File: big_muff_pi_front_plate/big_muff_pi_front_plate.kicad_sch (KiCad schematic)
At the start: 13 parts, among them J1 top_panel_connector

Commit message: Potentiometers checked, LED updated
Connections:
- net 0: now also J1.3 (GND)
- net at J1.5 (Pin_5): now also RV2.3; no longer RV2.1
- net at J1.9 (Pin_9): now also RV2.1; no longer RV2.3
- net at RV3.1: now also J1.16 (Pin_16); no longer J1.12 (Pin_12)
- net at RV3.3: now also J1.12 (Pin_12); no longer J1.16 (Pin_16)
- net 9V: now reaches J1.1 (VCC)
- net at J1.2 (Pin_2): now also RV1.3; no longer RV1.1
- net at J1.6 (Pin_6): now also RV1.1; no longer RV1.3
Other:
- moved on the sheet: RV1, RV2, RV3
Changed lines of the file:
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@@
+	(wire
+		(pts
+			(xy 238.76 124.46) (xy 236.22 124.46)
+		)
+		(stroke
+			(width 0)
+			(type default)
+		)
+	)
 	(wire
 		(pts
@@
 	(wire
 		(pts
+			(xy 236.22 124.46) (xy 236.22 128.27)
+		)
+		(stroke
+			(width 0)
+			(type default)
+		)
+	)
+	(wire
+		(pts
 			(xy 124.46 152.4) (xy 124.46 158.75)
 		)
@@
 			(width 0)
 			(type default)
+		)
+	)
+	(wire
+		(pts
+			(xy 236.22 140.97) (xy 236.22 144.78)
+		)
+		(stroke
+			(width 0)
+			(type default)
+		)
+	)
+	(global_label "9V"
+		(shape output)
+		(at 238.76 124.46 0)
+		(fields_autoplaced yes)
+		(effects
+			(font
+				(size 1.27 1.27)
+			)
+			(justify left)
+		)
+		(property "Intersheetrefs" "${INTERSHEET_REFS}"
+			(at 244.0433 124.46 0)
+			(effects
+				(font
+					(size 1.27 1.27)
+				)
+				(justify left)
+				(hide yes)
+			)
 		)
 	)
@@
 	)
 	(symbol
+		(lib_id "Simulation_SPICE:0")
+		(at 236.22 144.78 0)
+		(unit 1)
+		(exclude_from_sim no)
+		(in_bom yes)
+		(on_board yes)
+		(dnp no)
+		(fields_autoplaced yes)
+		(property "Reference" "#GND023"
+			(at 236.22 147.32 0)
+			(effects
+				(font
+					(size 1.27 1.27)
+				)
+				(hide yes)
+			)
+		)
+		(property "Value" "0"
+			(at 236.22 142.875 0)
+			(effects
+				(font
+					(size 1.27 1.27)
+				)
+				(hide yes)
+			)
+		)
+		(property "Footprint" ""
+			(at 236.22 144.78 0)
+			(effects
+				(font
+					(size 1.27 1.27)
+				)
+				(hide yes)
+			)
+		)
+		(property "Datasheet" "~"
+			(at 236.22 144.78 0)
+			(effects
+				(font
+					(size 1.27 1.27)
+				)
+				(hide yes)
+			)
+		)
+		(property "Description" ""
+			(at 236.22 144.78 0)
+			(effects
+				(font
+					(size 1.27 1.27)
+				)
+			)
+		)
+		(pin "1"
+		)
+		(instances
+			(project "big_muff_pi_front_plate"
+				(path "/1fda0e48-ac05-4486-b24b-352a2425b266"
+					(reference "#GND023")
+					(unit 1)
+				)
+			)
+		)
+	)
+	(symbol
 		(lib_id "Device:R_Potentiometer")
-		(at 54.61 77.47 0)
-		(mirror y)
+		(at 54.61 77.47 180)
 		(unit 1)
 		(exclude_from_sim no)
@@
 		(on_board yes)
 		(dnp no)
-		(fields_autoplaced yes)
 		(property "Reference" "RV3"
-			(at 57.15 76.1999 0)
+			(at 57.15 78.7401 0)
 			(effects
 				(font
@@
 		)
 		(property "Value" "R_Potentiometer"
-			(at 57.15 78.7399 0)
+			(at 57.15 76.2001 0)
 			(effects
 				(font
@@
 	(symbol
 		(lib_id "Device:R_Potentiometer")
-		(at 54.61 55.88 0)
-		(mirror y)
+		(at 54.61 55.88 180)
 		(unit 1)
 		(exclude_from_sim no)
@@
 		(on_board yes)
 		(dnp no)
-		(fields_autoplaced yes)
 		(property "Reference" "RV2"
-			(at 57.15 54.6099 0)
+			(at 57.15 57.1501 0)
 			(effects
 				(font
@@
 		)
 		(property "Value" "R_Potentiometer"
-			(at 57.15 57.1499 0)
+			(at 57.15 54.6101 0)
 			(effects
 				(font
@@
 	(symbol
 		(lib_id "Device:R_Potentiometer")
-		(at 54.61 33.02 0)
-		(mirror y)
+		(at 54.61 33.02 180)
 		(unit 1)
 		(exclude_from_sim no)
@@
 		(on_board yes)
 		(dnp no)
-		(fields_autoplaced yes)
 		(property "Reference" "RV1"
-			(at 57.15 31.7499 0)
+			(at 57.15 34.2901 0)
 			(effects
 				(font
@@
 		)
 		(property "Value" "R_Potentiometer"
-			(at 57.15 34.2899 0)
-			(effects
-				(font
+			(at 57.15 31.7501 0)
+			(effects
+				(font

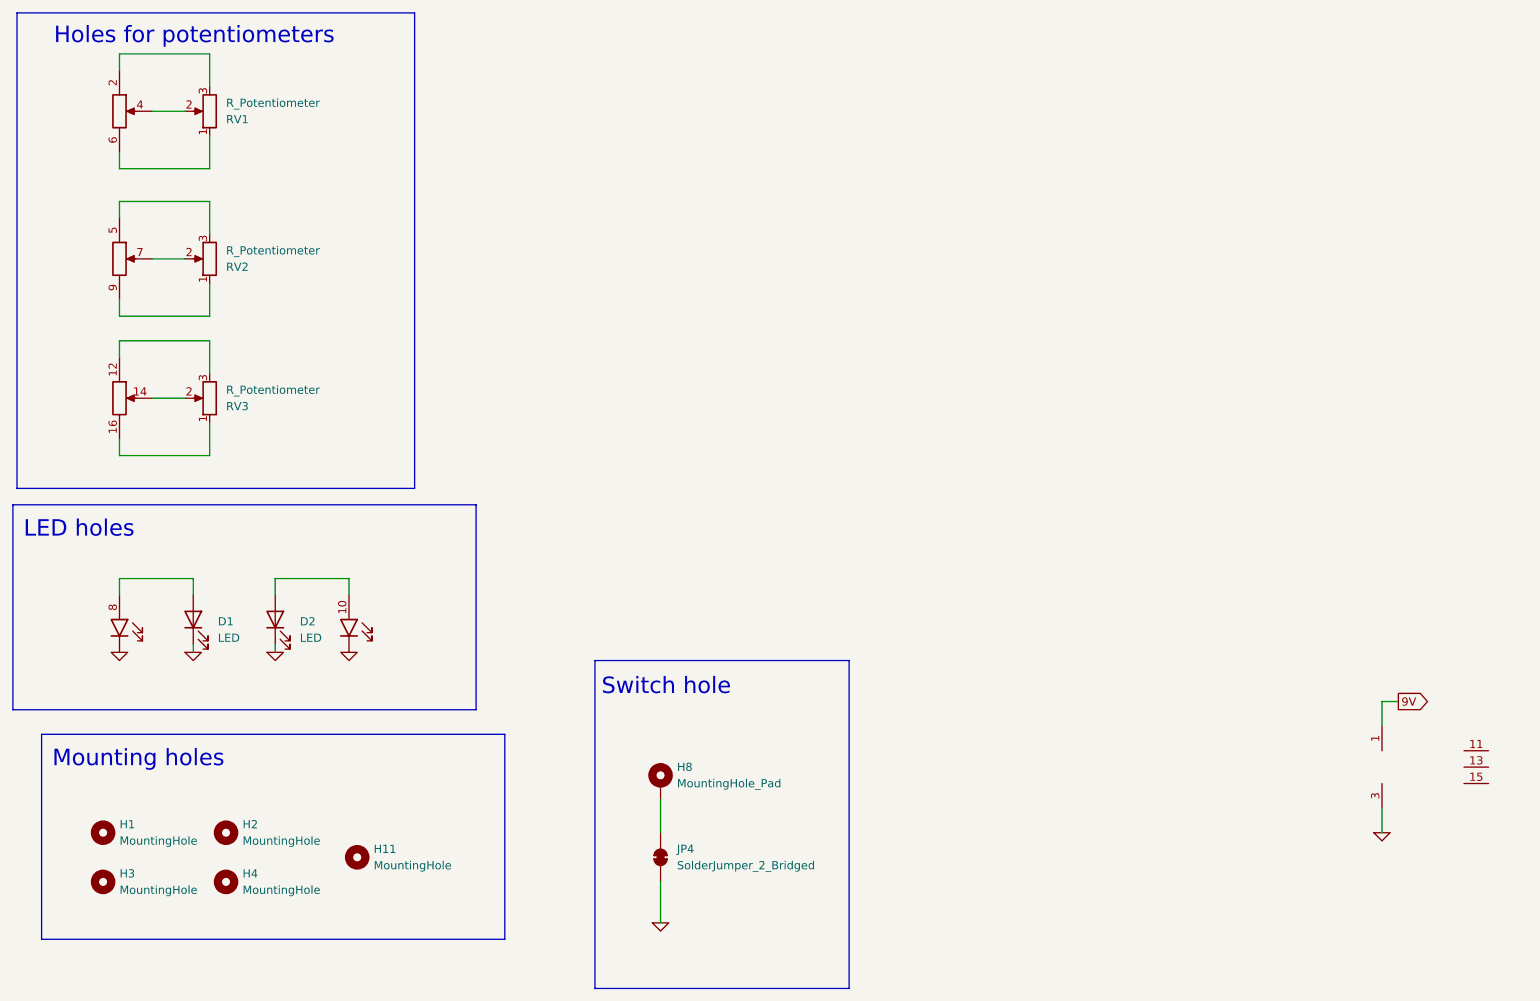
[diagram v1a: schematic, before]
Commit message: Front plate update.
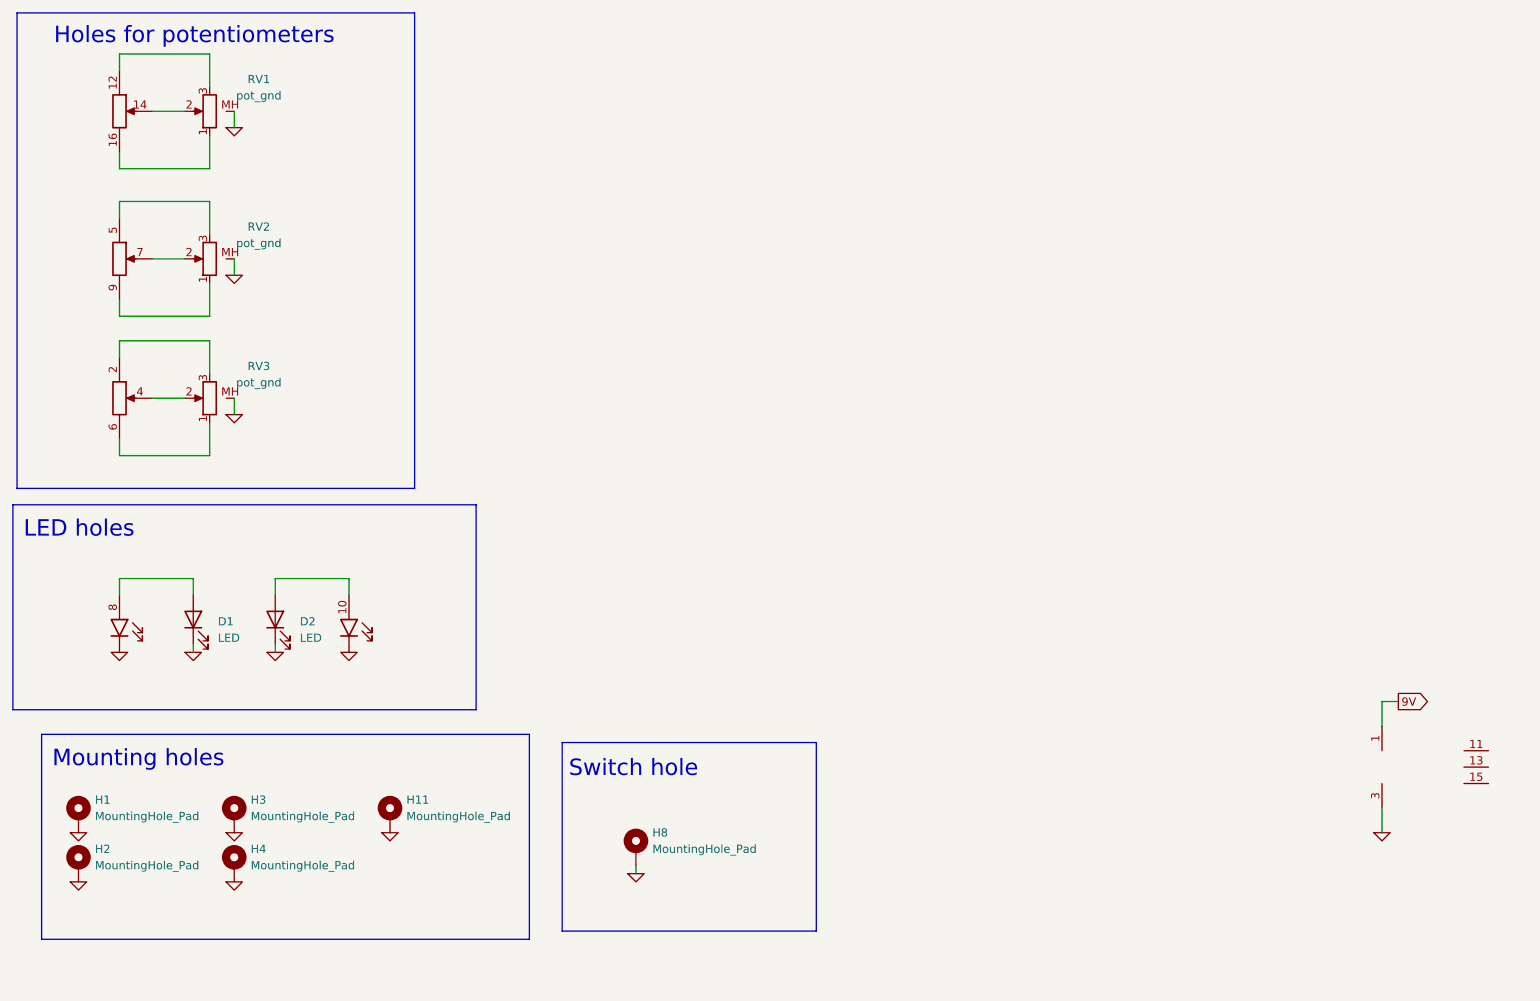
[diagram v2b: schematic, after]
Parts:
- removed H1, H11, H2, H3, H4: MountingHole, MountingHole:MountingHole_3.2mm_M3_DIN965_Pad_TopBottom, symbol Mechanical:MountingHole
- removed JP4: SolderJumper_2_Bridged, Jumper:SolderJumper-2_P1.3mm_Bridged_RoundedPad1.0x1.5mm, symbol Jumper:SolderJumper_2_Bridged
- removed RV1, RV2, RV3: R_Potentiometer, pedale:top_plate_pot, symbol Device:R_Potentiometer
- added H1, H11, H2, H3, H4: MountingHole_Pad, MountingHole:MountingHole_3.2mm_M3_DIN965_Pad_TopBottom, symbol Mechanical:MountingHole_Pad
- added RV1, RV2, RV3: pot_gnd, pedale:top_plate_pot, symbol pedale:pot_gnd
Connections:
- net 0: now also H8.1, H1.1, H11.1, H2.1, H3.1, H4.1, RV1.MH (2), RV2.MH (2), RV3.MH (2)
- net at J1.5 (Pin_5): now also RV2.3
- net at J1.7 (Pin_7): now also RV2.2
- net at J1.9 (Pin_9): now also RV2.1
- net at J1.16 (Pin_16): now also RV1.1
- net at J1.14 (Pin_14): now also RV1.2
- net at J1.12 (Pin_12): now also RV1.3
- net at J1.2 (Pin_2): now also RV3.3
- net at J1.4 (Pin_4): now also RV3.2
- net at J1.6 (Pin_6): now also RV3.1
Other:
- moved on the sheet: H8

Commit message: Big muff pi, new connector position.
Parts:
- J1: footprint pedale:bottom_connector -> Connector_IDC:IDC-Header_2x08_P2.54mm_Vertical
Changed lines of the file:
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@@
 			)
 		)
-		(property "Footprint" "pedale:bottom_connector"
+		(property "Footprint" "Connector_IDC:IDC-Header_2x08_P2.54mm_Vertical"
 			(at 40.64 55.88 0)
 			(effects
@@
 			)
 		)
-		(property "Datasheet" "~"
+		(property "Datasheet" "https://ngspice.sourceforge.io/docs/ngspice-html-manual/manual.xhtml#subsec_Circuit_elements__device"
 			(at 236.22 144.78 0)
 			(effects
@@
 			)
 		)
-		(property "Description" ""
+		(property "Description" "0V reference potential for simulation"
 			(at 236.22 144.78 0)
 			(effects
@@
 			)
 		)
-		(property "Footprint" "pedale:bottom_connector"
+		(property "Footprint" "Connector_IDC:IDC-Header_2x08_P2.54mm_Vertical"
 			(at 236.22 140.97 0)
 			(effects
@@
 			)
 		)
-		(property "Footprint" "pedale:bottom_connector"
+		(property "Footprint" "Connector_IDC:IDC-Header_2x08_P2.54mm_Vertical"
 			(at 40.64 33.02 0)
 			(effects
@@
 			)
 		)
-		(property "Footprint" "pedale:bottom_connector"
+		(property "Footprint" "Connector_IDC:IDC-Header_2x08_P2.54mm_Vertical"
 			(at 76.2 113.03 0)
 			(effects
@@
 			)
 		)
-		(property "Footprint" "pedale:bottom_connector"
+		(property "Footprint" "Connector_IDC:IDC-Header_2x08_P2.54mm_Vertical"
 			(at 40.64 113.03 0)
 			(effects
@@
 			)
 		)
-		(property "Footprint" "pedale:bottom_connector"
+		(property "Footprint" "Connector_IDC:IDC-Header_2x08_P2.54mm_Vertical"
 			(at 248.92 137.16 0)
 			(effects
@@
 			)
 		)
-		(property "Footprint" "pedale:bottom_connector"
+		(property "Footprint" "Connector_IDC:IDC-Header_2x08_P2.54mm_Vertical"
 			(at 40.64 77.47 0)
 			(effects

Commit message: Front plate update, componets created.
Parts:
- J1: footprint Connector_IDC:IDC-Header_2x08_P2.54mm_Vertical -> pedale:IDC-Header_2x08_faux_SMD
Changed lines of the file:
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@@
 			)
 		)
-		(property "Footprint" "Connector_IDC:IDC-Header_2x08_P2.54mm_Vertical"
+		(property "Footprint" "pedale:IDC-Header_2x08_faux_SMD"
 			(at 40.64 55.88 0)
 			(effects
@@
 			)
 		)
-		(property "Footprint" "Connector_IDC:IDC-Header_2x08_P2.54mm_Vertical"
+		(property "Footprint" "pedale:IDC-Header_2x08_faux_SMD"
 			(at 236.22 140.97 0)
 			(effects
@@
 			)
 		)
-		(property "Footprint" "Connector_IDC:IDC-Header_2x08_P2.54mm_Vertical"
+		(property "Footprint" "pedale:IDC-Header_2x08_faux_SMD"
 			(at 40.64 33.02 0)
 			(effects
@@
 			)
 		)
-		(property "Footprint" "Connector_IDC:IDC-Header_2x08_P2.54mm_Vertical"
+		(property "Footprint" "pedale:IDC-Header_2x08_faux_SMD"
 			(at 76.2 113.03 0)
 			(effects
@@
 			)
 		)
-		(property "Footprint" "Connector_IDC:IDC-Header_2x08_P2.54mm_Vertical"
+		(property "Footprint" "pedale:IDC-Header_2x08_faux_SMD"
 			(at 40.64 113.03 0)
 			(effects
@@
 			)
 		)
-		(property "Footprint" "Connector_IDC:IDC-Header_2x08_P2.54mm_Vertical"
+		(property "Footprint" "pedale:IDC-Header_2x08_faux_SMD"
 			(at 248.92 137.16 0)
 			(effects
@@
 			)
 		)
-		(property "Footprint" "Connector_IDC:IDC-Header_2x08_P2.54mm_Vertical"
+		(property "Footprint" "pedale:IDC-Header_2x08_faux_SMD"
 			(at 40.64 77.47 0)
 			(effects
